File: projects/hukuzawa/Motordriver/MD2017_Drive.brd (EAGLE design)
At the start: 70 x 70 mm, 22 parts

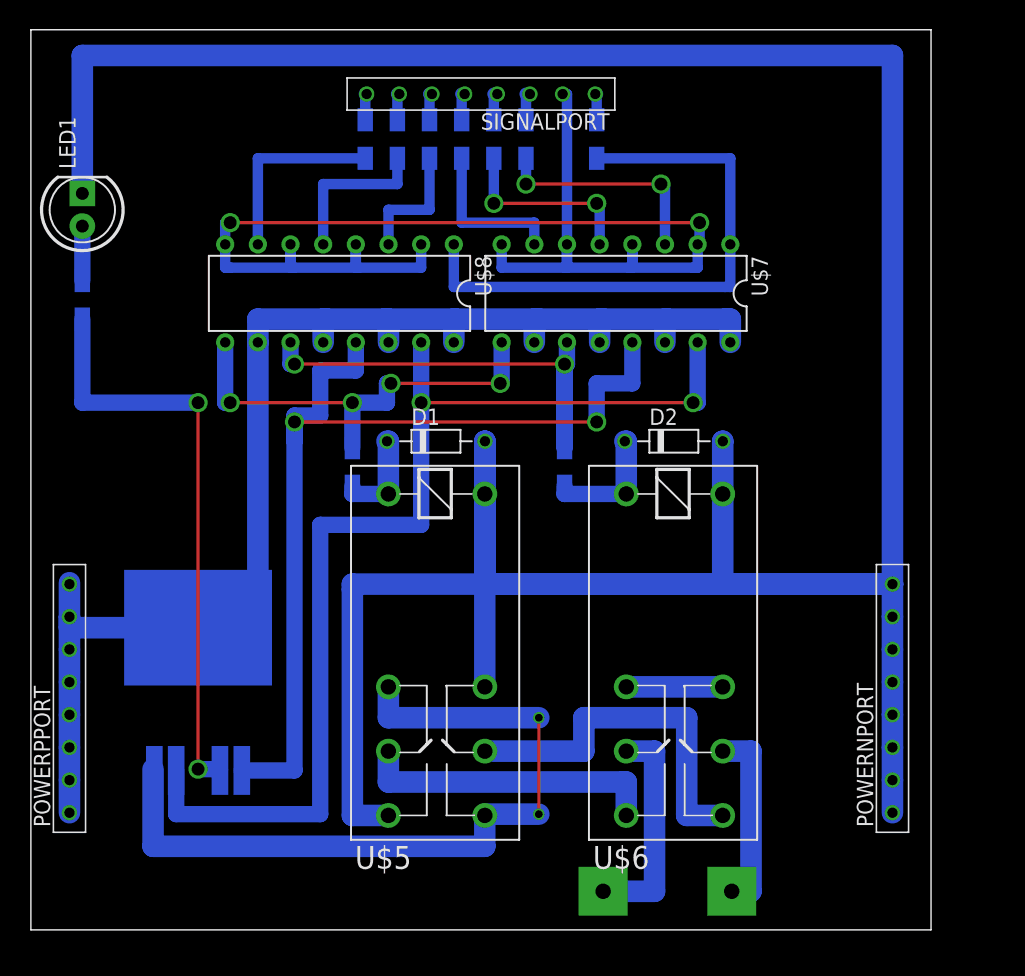
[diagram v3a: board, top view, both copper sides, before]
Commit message: モータードライバデータ修正
ドリル径の修正、それに伴う配置の若干の変更
ダイオードのライブラリの修正
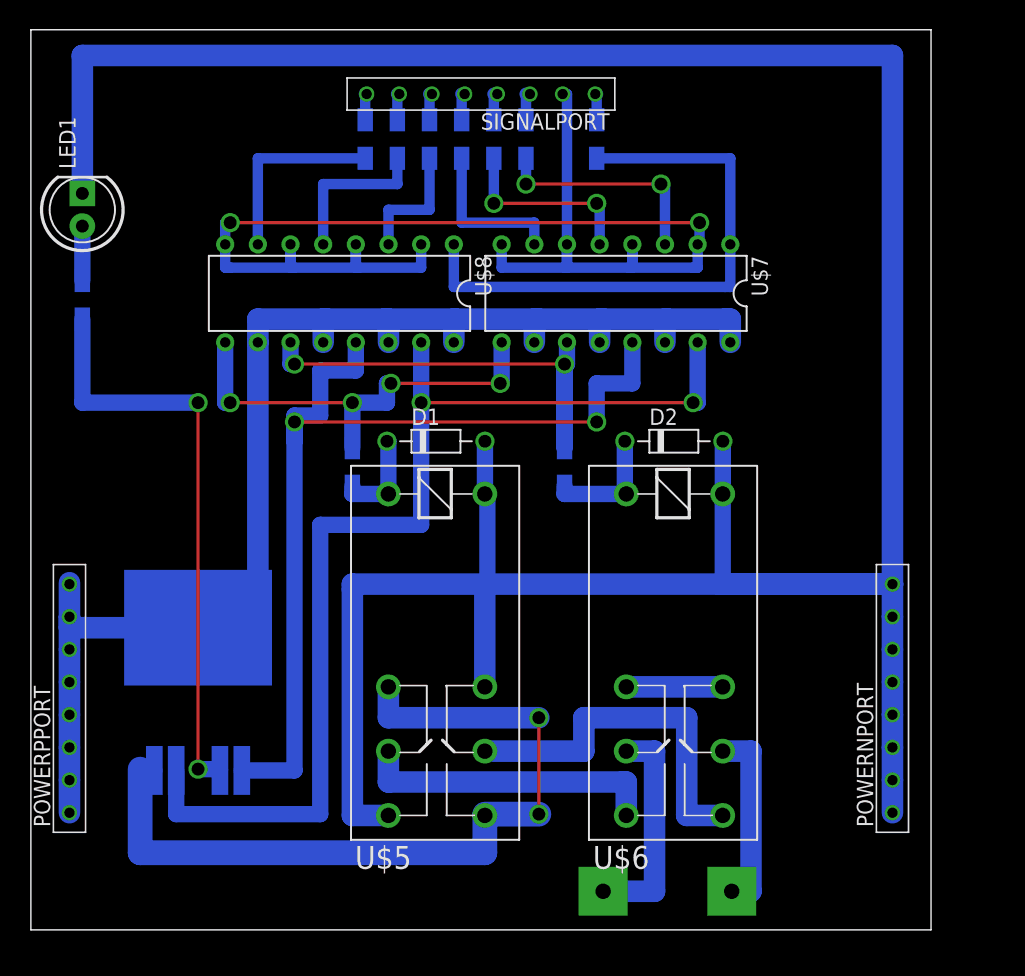
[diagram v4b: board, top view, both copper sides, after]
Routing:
- net GND-D: track 281.6 -> 240.1 mm
- net N$2: track 60.3 -> 63.3 mm
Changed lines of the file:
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@@
 <element name="U$7" library="photocoupler" package="16PIN" value="TLP521-4" x="45.5" y="49.5" rot="R180"/>
 <element name="U$8" library="photocoupler" package="16PIN" value="TLP521-4" x="24" y="49.5" rot="R180"/>
-<element name="D1" library="diode" package="DIODE7.5" value="" x="31.5" y="38"/>
-<element name="D2" library="diode" package="DIODE7.5" value="" x="50" y="38"/>
 <element name="LED1" library="FP-21T for MITS" package="LED5MM" value="" x="4" y="56" rot="R90"/>
 <element name="R1" library="rcl" package="R3216W" value="" x="4" y="49" rot="MR270"/>
@@
 <element name="R9" library="rcl" package="R3216W" value="" x="25" y="36" rot="MR90"/>
 <element name="R10" library="rcl" package="R3216W" value="" x="41.5" y="36" rot="MR90"/>
+<element name="D1" library="diode" package="DIODE7.5" value="" x="31.5" y="38"/>
+<element name="D2" library="diode" package="DIODE7.5" value="" x="50" y="38"/>
 </elements>
 <signals>
@@
 </signal>
 <signal name="GND-D">
-<contactref element="D2" pad="PA"/>
 <contactref element="U$6" pad="8"/>
-<contactref element="D1" pad="PA"/>
 <contactref element="U$5" pad="8"/>
 <contactref element="LED1" pad="K"/>
@@
 <contactref element="POWERNPORT" pad="7"/>
 <contactref element="POWERNPORT" pad="8"/>
-<wire x1="53.8" y1="33.9" x2="53.8" y2="38" width="1.6764" layer="16"/>
-<wire x1="53.8" y1="38" x2="53.81" y2="38" width="1.6764" layer="16"/>
-<wire x1="35.3" y1="33.9" x2="35.3" y2="38" width="1.6764" layer="16"/>
-<wire x1="35.3" y1="38" x2="35.31" y2="38" width="1.6764" layer="16"/>
 <wire x1="4" y1="57.27" x2="4" y2="68" width="1.6764" layer="16"/>
 <wire x1="4" y1="68" x2="67" y2="68" width="1.6764" layer="16"/>
@@
 <contactref element="U$5" pad="4"/>
 <contactref element="U$5" pad="7"/>
-<wire x1="35.3" y1="33.9" x2="35.3" y2="18.9" width="1.6764" layer="16"/>
-<wire x1="53.8" y1="33.9" x2="53.8" y2="26.89" width="1.6764" layer="16"/>
 <wire x1="53.8" y1="26.89" x2="67" y2="26.89" width="1.6764" layer="16"/>
-<wire x1="35.31" y1="38" x2="35.31" y2="26.89" width="1.6764" layer="16"/>
-<wire x1="35.31" y1="26.89" x2="67" y2="26.89" width="1.6764" layer="16"/>
 <wire x1="27.8" y1="8.9" x2="25" y2="8.9" width="1.6764" layer="16"/>
 <wire x1="25" y1="8.9" x2="25" y2="26.5" width="1.6764" layer="16"/>
 <wire x1="25" y1="26.5" x2="25" y2="26.89" width="1.6764" layer="16"/>
-<wire x1="25" y1="26.89" x2="67" y2="26.89" width="1.6764" layer="16"/>
+<wire x1="25" y1="26.89" x2="35.5" y2="26.89" width="1.6764" layer="16"/>
+<wire x1="35.5" y1="26.89" x2="53.5" y2="26.89" width="1.6764" layer="16"/>
+<wire x1="53.5" y1="26.89" x2="67" y2="26.89" width="1.6764" layer="16"/>
 <wire x1="67" y1="26.89" x2="67" y2="24.35" width="1.6764" layer="16"/>
 <wire x1="67" y1="24.35" x2="67" y2="21.81" width="1.6764" layer="16"/>
@@
 <wire x1="67" y1="14.19" x2="67" y2="11.65" width="1.6764" layer="16"/>
 <wire x1="67" y1="11.65" x2="67" y2="9.11" width="1.6764" layer="16"/>
+<contactref element="D1" pad="PA"/>
+<contactref element="D2" pad="PA"/>
+<wire x1="35.3" y1="33.9" x2="35.31" y2="33.9" width="1.27" layer="16"/>
+<wire x1="35.31" y1="33.9" x2="35.31" y2="38" width="1.27" layer="16"/>
+<wire x1="35.3" y1="33.9" x2="35.5" y2="33.9" width="1.27" layer="16"/>
+<wire x1="35.3" y1="18.9" x2="35.3" y2="26.5" width="1.6764" layer="16"/>
+<wire x1="35.3" y1="26.5" x2="35.3" y2="26.89" width="1.6764" layer="16"/>
+<wire x1="35.3" y1="26.89" x2="35.5" y2="26.89" width="1.6764" layer="16"/>
+<wire x1="53.8" y1="33.9" x2="53.81" y2="33.9" width="1.27" layer="16"/>
+<wire x1="53.81" y1="33.9" x2="53.81" y2="38" width="1.27" layer="16"/>
+<wire x1="53.8" y1="33.9" x2="53.8" y2="26.89" width="1.27" layer="16"/>
+<wire x1="53.8" y1="26.89" x2="53.5" y2="26.89" width="1.27" layer="16"/>
+<wire x1="35.5" y1="33.9" x2="35.5" y2="26.5" width="1.27" layer="16"/>
+<wire x1="35.5" y1="26.5" x2="35.3" y2="26.5" width="1.27" layer="16"/>
 </signal>
 <signal name="BDIR">
@@
 <contactref element="U$5" pad="2"/>
 <wire x1="35.3" y1="8.9" x2="35.3" y2="9" width="1.6764" layer="16"/>
-<wire x1="35.3" y1="9" x2="39.5" y2="9" width="1.6764" layer="16"/>
-<via x="39.5" y="9" extent="1-16" drill="0.6" shape="square"/>
+<wire x1="35.3" y1="9" x2="39.5" y2="9" width="1.9304" layer="16"/>
+<via x="39.5" y="9" extent="1-16" drill="1"/>
 <wire x1="39.5" y1="9" x2="39.5" y2="16.5" width="0.254" layer="1"/>
-<via x="39.5" y="16.5" extent="1-16" drill="0.6" shape="square"/>
+<via x="39.5" y="16.5" extent="1-16" drill="1"/>
 <wire x1="39.5" y1="16.5" x2="27.8" y2="16.5" width="1.6764" layer="16"/>
 <wire x1="27.8" y1="16.5" x2="27.8" y2="18.9" width="1.6764" layer="16"/>
-<wire x1="9.6" y1="12.4" x2="9.5" y2="12.4" width="1.016" layer="16"/>
-<wire x1="9.5" y1="12.4" x2="9.5" y2="12.5" width="1.016" layer="16"/>
-<wire x1="9.5" y1="12.5" x2="9.5" y2="6.5" width="1.6764" layer="16"/>
-<wire x1="9.5" y1="6.5" x2="35" y2="6.5" width="1.6764" layer="16"/>
-<wire x1="35" y1="6.5" x2="35.3" y2="6.5" width="1.6764" layer="16"/>
-<wire x1="35.3" y1="6.5" x2="35.3" y2="8.9" width="1.6764" layer="16"/>
+<wire x1="9.6" y1="12.4" x2="8.5" y2="12.4" width="1.27" layer="16"/>
+<wire x1="8.5" y1="12.4" x2="8.5" y2="12.5" width="1.27" layer="16"/>
+<wire x1="8.5" y1="12.5" x2="8.5" y2="6" width="1.9304" layer="16"/>
+<wire x1="8.5" y1="6" x2="35.3" y2="6" width="1.9304" layer="16"/>
+<wire x1="35.3" y1="6" x2="35.3" y2="8.9" width="1.9304" layer="16"/>
 </signal>
 <signal name="N$3">
@@
 <signal name="N$9">
 <contactref element="U$5" pad="1"/>
+<contactref element="R9" pad="1"/>
 <contactref element="D1" pad="PK"/>
-<contactref element="R9" pad="1"/>
-<wire x1="27.8" y1="33.9" x2="27.8" y2="38" width="1.6764" layer="16"/>
-<wire x1="27.8" y1="38" x2="27.69" y2="38" width="1.6764" layer="16"/>
-<wire x1="25" y1="34.501" x2="25" y2="33.9" width="1.27" layer="16"/>
-<wire x1="25" y1="33.9" x2="27.8" y2="33.9" width="1.27" layer="16"/>
+<wire x1="27.69" y1="38" x2="27.8" y2="38" width="1.27" layer="16"/>
+<wire x1="27.8" y1="38" x2="27.8" y2="33.9" width="1.27" layer="16"/>
+<wire x1="27.8" y1="33.9" x2="25" y2="33.9" width="1.27" layer="16"/>
+<wire x1="25" y1="33.9" x2="25" y2="34.501" width="1.27" layer="16"/>
 </signal>
 <signal name="11">
 <contactref element="U$6" pad="1"/>
-<contactref element="D2" pad="PK"/>
-<wire x1="46.3" y1="33.9" x2="46.3" y2="38" width="1.6764" layer="16"/>
-<wire x1="46.3" y1="38" x2="46.19" y2="38" width="1.6764" layer="16"/>
 <contactref element="R10" pad="1"/>
 <wire x1="46.3" y1="33.9" x2="41.5" y2="33.9" width="1.27" layer="16"/>
 <wire x1="41.5" y1="33.9" x2="41.5" y2="34.501" width="1.27" layer="16"/>
+<contactref element="D2" pad="PK"/>
+<wire x1="46.3" y1="33.9" x2="46.19" y2="33.9" width="1.27" layer="16"/>
+<wire x1="46.19" y1="33.9" x2="46.19" y2="38" width="1.27" layer="16"/>
 </signal>
 <signal name="D/B">

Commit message: モータードライバ修正
Base,Space: 基板の無駄であるため削除
Drive: 基板固定用の穴を追加
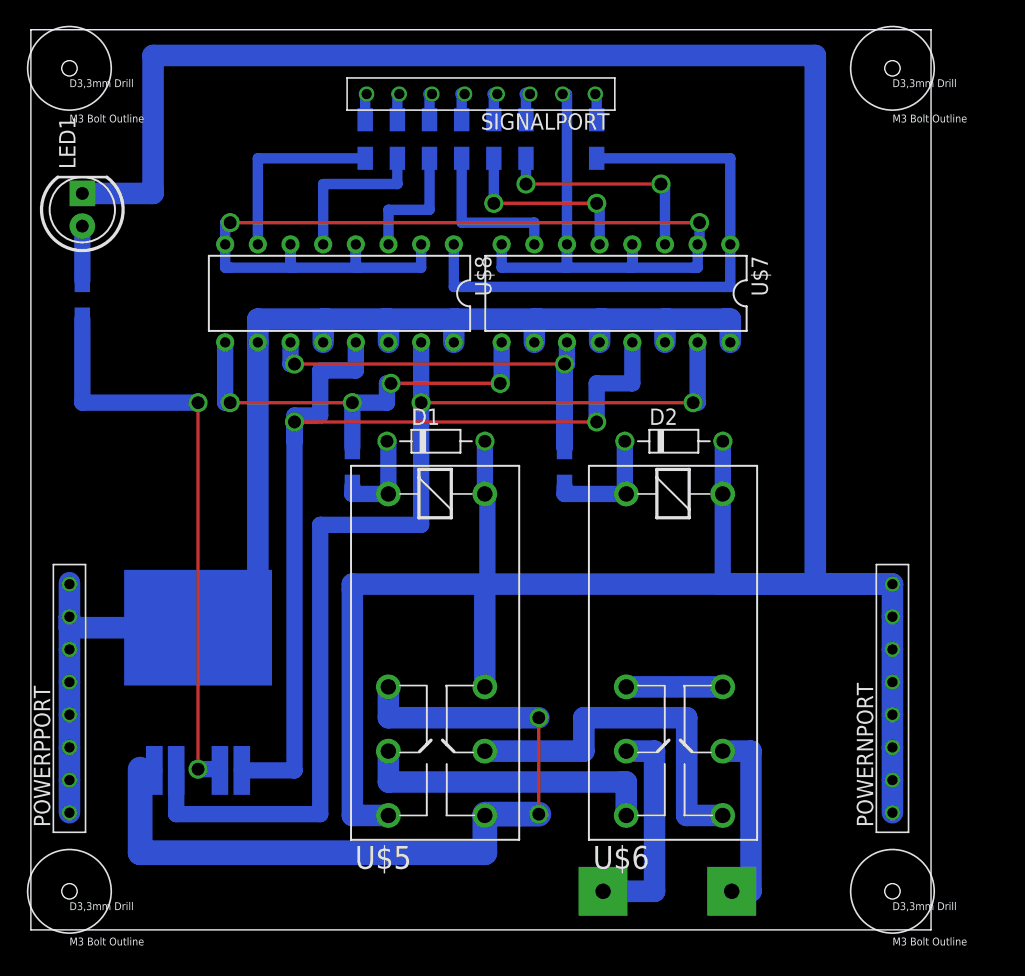
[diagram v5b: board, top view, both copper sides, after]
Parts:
- added U$1, U$10, U$2, U$3: (no value), FP-21T for MITS:HOLE3.3
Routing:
- net GND-D: track 240.1 -> 234.1 mm
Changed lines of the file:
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@@
 <element name="D1" library="diode" package="DIODE7.5" value="" x="31.5" y="38"/>
 <element name="D2" library="diode" package="DIODE7.5" value="" x="50" y="38"/>
+<element name="U$1" library="FP-21T for MITS" package="HOLE3.3" value="" x="3" y="67"/>
+<element name="U$2" library="FP-21T for MITS" package="HOLE3.3" value="" x="67" y="67"/>
+<element name="U$3" library="FP-21T for MITS" package="HOLE3.3" value="" x="3" y="3"/>
+<element name="U$10" library="FP-21T for MITS" package="HOLE3.3" value="" x="67" y="3"/>
 </elements>
 <signals>
@@
 <contactref element="POWERNPORT" pad="7"/>
 <contactref element="POWERNPORT" pad="8"/>
-<wire x1="4" y1="57.27" x2="4" y2="68" width="1.6764" layer="16"/>
-<wire x1="4" y1="68" x2="67" y2="68" width="1.6764" layer="16"/>
-<wire x1="67" y1="68" x2="67" y2="26.89" width="1.6764" layer="16"/>
 <contactref element="U$5" pad="4"/>
 <contactref element="U$5" pad="7"/>
-<wire x1="53.8" y1="26.89" x2="67" y2="26.89" width="1.6764" layer="16"/>
+<wire x1="53.8" y1="26.89" x2="61" y2="26.89" width="1.6764" layer="16"/>
+<wire x1="61" y1="26.89" x2="67" y2="26.89" width="1.6764" layer="16"/>
 <wire x1="27.8" y1="8.9" x2="25" y2="8.9" width="1.6764" layer="16"/>
 <wire x1="25" y1="8.9" x2="25" y2="26.5" width="1.6764" layer="16"/>
@@
 <wire x1="25" y1="26.89" x2="35.5" y2="26.89" width="1.6764" layer="16"/>
 <wire x1="35.5" y1="26.89" x2="53.5" y2="26.89" width="1.6764" layer="16"/>
-<wire x1="53.5" y1="26.89" x2="67" y2="26.89" width="1.6764" layer="16"/>
+<wire x1="53.5" y1="26.89" x2="61" y2="26.89" width="1.6764" layer="16"/>
+<wire x1="61" y1="26.89" x2="67" y2="26.89" width="1.6764" layer="16"/>
 <wire x1="67" y1="26.89" x2="67" y2="24.35" width="1.6764" layer="16"/>
 <wire x1="67" y1="24.35" x2="67" y2="21.81" width="1.6764" layer="16"/>
@@
 <wire x1="35.5" y1="33.9" x2="35.5" y2="26.5" width="1.27" layer="16"/>
 <wire x1="35.5" y1="26.5" x2="35.3" y2="26.5" width="1.27" layer="16"/>
+<wire x1="9.5" y1="68" x2="9.5" y2="57.5" width="1.6764" layer="16"/>
+<wire x1="9.5" y1="57.5" x2="9.5" y2="57.27" width="1.6764" layer="16"/>
+<wire x1="9.5" y1="57.27" x2="4" y2="57.27" width="1.6764" layer="16"/>
+<wire x1="9.5" y1="68" x2="61" y2="68" width="1.6764" layer="16"/>
+<wire x1="61" y1="68" x2="61" y2="26.89" width="1.6764" layer="16"/>
 </signal>
 <signal name="BDIR">

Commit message: モータードライバ全ボード図修正
配置の基準単位をmilに変更して再配置・再配線
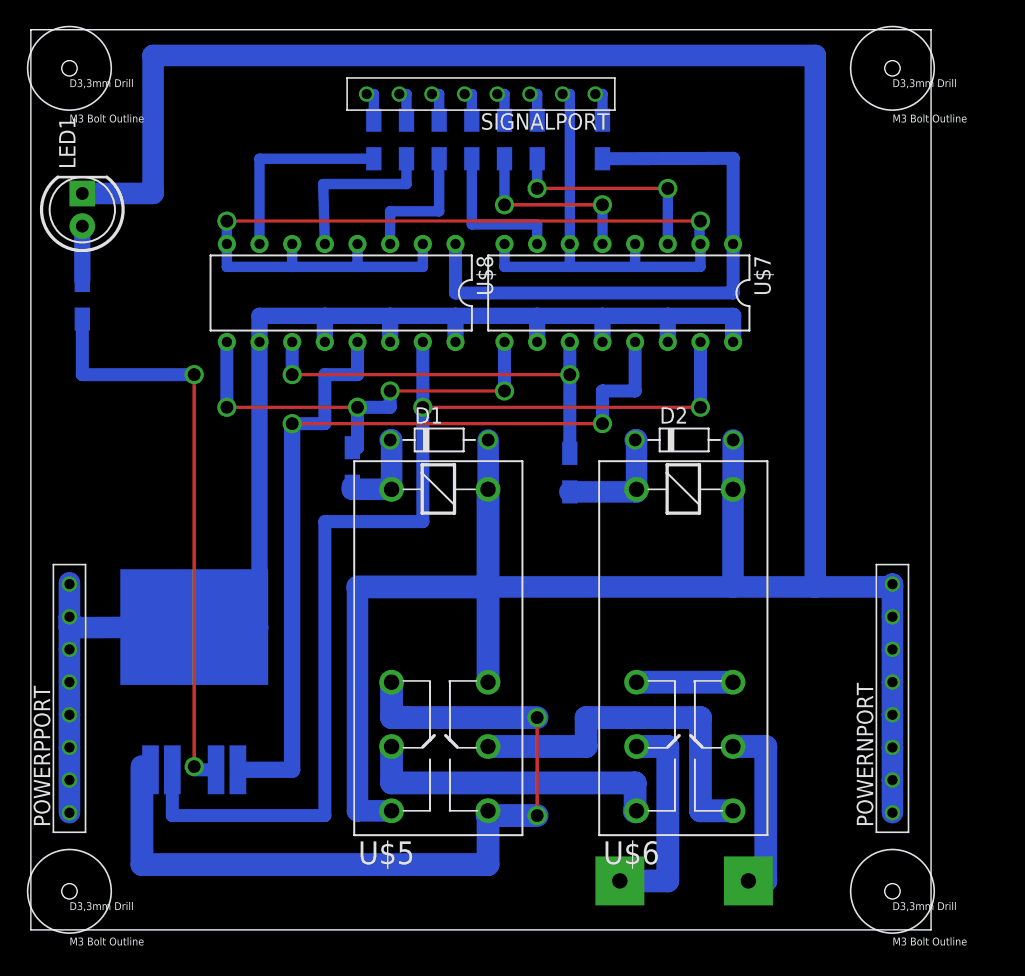
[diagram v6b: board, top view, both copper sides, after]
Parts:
- removed U$4: BUK116-50L, BUK116-50L:BUK116-50L
- added FET1: BUK116-50L, BUK116-50L:BUK116-50L
- R2, R3, R4, R5, R6, R7, R8: value (none) -> 300
- moved U$9 1.53 mm to (50.8, 3.81)
- moved U$6 0.88 mm to (50.8, 22.9)
- moved R3 0.87 mm to (39.4, 61.5)
- moved R4 0.83 mm to (36.8, 61.5)
- moved D2 0.81 mm to (50.8, 38.1)
- moved R5 0.79 mm to (34.3, 61.5)
- moved R6 0.75 mm to (31.8, 61.5)
- moved R7 0.71 mm to (29.2, 61.5)
- moved R8 0.67 mm to (26.7, 61.5)
- moved R10 0.60 mm to (41.9, 35.6)
- moved R2 0.45 mm to (44.5, 61.5)
- moved U$5 0.44 mm to (31.8, 22.9)
- moved D1 0.27 mm to (31.8, 38.1)
- moved U$7 0.22 mm to (45.7, 49.5)
- moved U$8 0.13 mm to (24.1, 49.5)
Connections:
- net N$1 renamed BRAKES
- net N$3 renamed DIRP
- net N$4 renamed DIRN
- net N$5 renamed OUTN
- net N$6 renamed OUTP
- removed net N$10: U$4.4, U$7.15, U$8.15
- removed net N$2: U$4.5, U$5.2, U$5.5
- new net PROTECTSP.: FET1.4, U$7.15, U$8.15
- new net PWMOUT: FET1.5, U$5.2, U$5.5
- net N$7: now also FET1.2; no longer U$4.2
- net PWM: now also FET1.1; no longer U$4.1
- net VCC12V: now also FET1.3; no longer U$4.3
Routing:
- net N$10: track 86.8 -> 0.00 mm, vias 2 -> 0
- net PROTECTSP.: track 0.00 -> 86.5 mm, vias 0 -> 2
- net PWMOUT: track 0.00 -> 65.5 mm, vias 0 -> 2
- net N$2: track 63.3 -> 0.00 mm, vias 2 -> 0
- net GND-D: track 234.1 -> 219.1 mm
- net GND-C: track 104.7 -> 97.5 mm
- net D/B: track 37.9 -> 32.8 mm
- net PWM: track 79.1 -> 75.6 mm
- net DIR: track 34.4 -> 35.3 mm
- net 8: track 45.2 -> 46.0 mm
- net 7: track 17.5 -> 16.8 mm
- net 6: track 14.9 -> 14.2 mm
- net 3: track 12.5 -> 13.1 mm
- net 5: track 12.3 -> 11.7 mm
- net 4: track 9.88 -> 10.4 mm
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
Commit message: モータードライバ修正
すべての配線の名前を変更
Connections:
- net 11 renamed NDSUPP2
- net 2 renamed NSIG6
- net 3 renamed NSIG5
- net 4 renamed NSIG4
- net 5 renamed NSIG3
- net 6 renamed NSIG2
- net 7 renamed NSIG1
- net 8 renamed NCSUPP1
- net N$9 renamed NDSUPP1
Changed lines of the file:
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@@
 </elements>
 <signals>
-<signal name="8">
+<signal name="NCSUPP1">
 <contactref element="U$7" pad="1"/>
 <contactref element="U$8" pad="1"/>
@@
 <wire x1="52" y1="55.118" x2="52.07" y2="55.118" width="0.8128" layer="16"/>
 </signal>
-<signal name="7">
+<signal name="NSIG1">
 <contactref element="U$7" pad="3"/>
 <contactref element="R3" pad="1"/>
@@
 <wire x1="49.53" y1="57.658" x2="49.53" y2="53.34" width="0.8128" layer="16"/>
 </signal>
-<signal name="6">
+<signal name="NSIG2">
 <contactref element="U$7" pad="5"/>
 <contactref element="R4" pad="1"/>
@@
 <wire x1="44.45" y1="56.388" x2="44.45" y2="53.34" width="0.8128" layer="16"/>
 </signal>
-<signal name="5">
+<signal name="NSIG3">
 <contactref element="U$7" pad="7"/>
 <contactref element="R5" pad="1"/>
@@
 <wire x1="34.29" y1="54.864" x2="34.29" y2="59.969" width="0.8128" layer="16"/>
 </signal>
-<signal name="4">
+<signal name="NSIG4">
 <contactref element="U$8" pad="3"/>
 <contactref element="R6" pad="1"/>
@@
 <wire x1="31.75" y1="55.88" x2="31.75" y2="59.969" width="0.8128" layer="16"/>
 </signal>
-<signal name="3">
+<signal name="NSIG5">
 <contactref element="U$8" pad="5"/>
 <contactref element="R7" pad="1"/>
@@
 <wire x1="29.21" y1="58" x2="29.21" y2="59.969" width="0.8128" layer="16"/>
 </signal>
-<signal name="2">
+<signal name="NSIG6">
 <contactref element="U$8" pad="7"/>
 <contactref element="R8" pad="1"/>
@@
 <wire x1="49.53" y1="45.72" x2="49.53" y2="47.752" width="1.27" layer="16"/>
 </signal>
-<signal name="N$9">
+<signal name="NDSUPP1">
 <contactref element="U$5" pad="1"/>
 <contactref element="R9" pad="1"/>
@@
 <wire x1="25" y1="34.26" x2="25" y2="34.501" width="1.6764" layer="16"/>
 </signal>
-<signal name="11">
+<signal name="NDSUPP2">
 <contactref element="U$6" pad="1"/>
 <contactref element="R10" pad="1"/>
